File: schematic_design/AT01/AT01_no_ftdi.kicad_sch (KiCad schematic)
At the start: 66 parts, among them J1 JST Connector, J2 USB_C_Receptacle_USB2.0, J3 Conn_01x08, J4 Solenoid Valve Connector, J5 DC Pump Connector, Q1 DMG2301L, Q2 FDS6375, SW1 SW_Push, SW2 SW_Push, SW3 SW_Push, SW4 SW_Push, U1 MPRLS0025PA00001A, U2 LT1935ES5-TRPBF, U3 MCP73844T-840I/MS, U4 LM1117MP-3.3, U5 DRV8833PW, U6 ESP32-WROOM-32

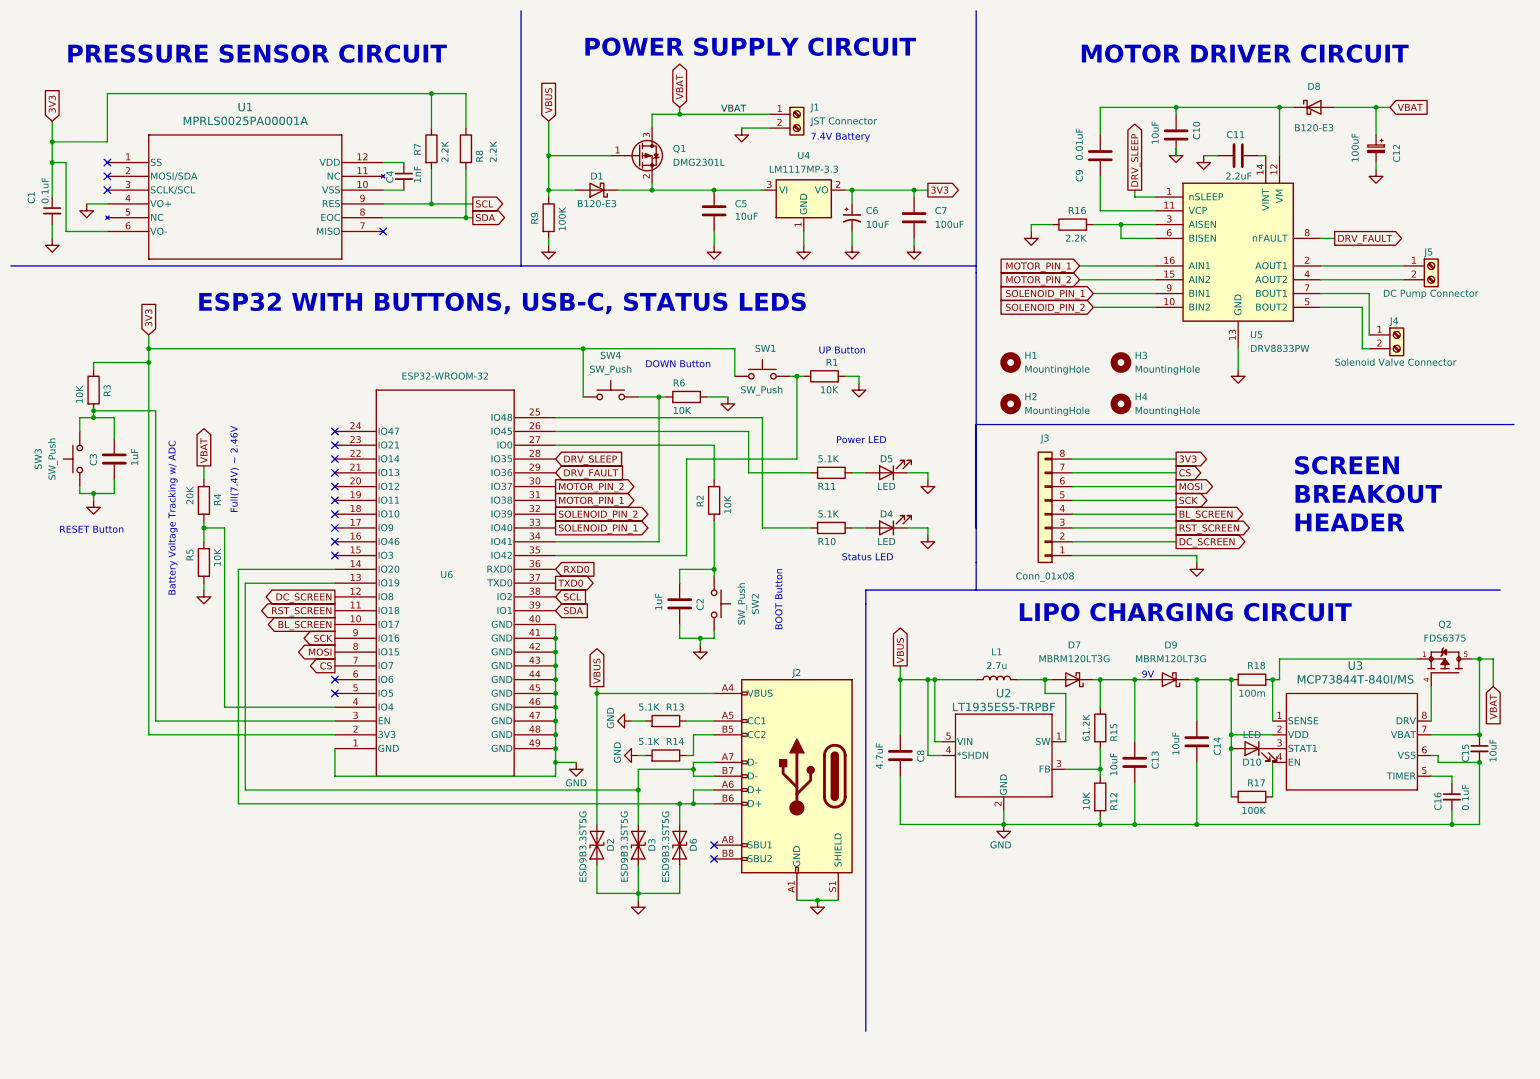
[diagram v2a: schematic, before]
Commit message: PCB redesign for new charging circuit with Espressif recommendations
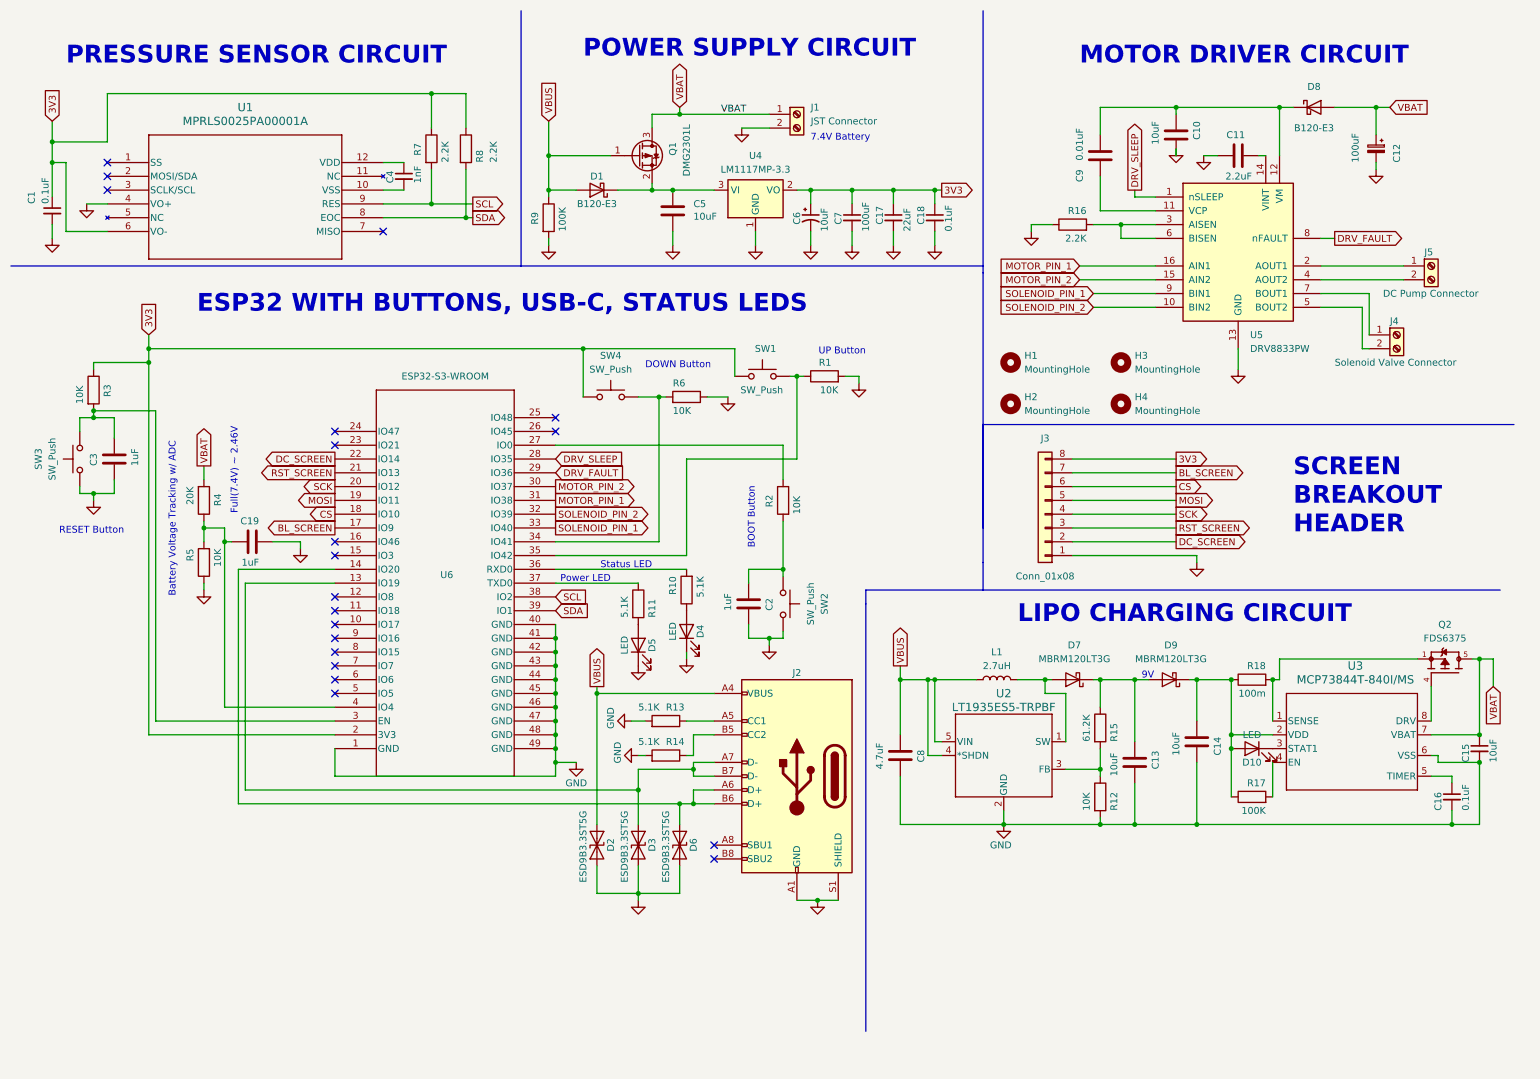
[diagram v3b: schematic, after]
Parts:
- removed C7: 100uF, Capacitor_SMD:C_0603_1608Metric_Pad1.08x0.95mm_HandSolder, symbol Device:C
- added C17: 22uF, Capacitor_SMD:C_0603_1608Metric_Pad1.08x0.95mm_HandSolder, symbol Device:C_Small
- added C18: 0.1uF, Capacitor_SMD:C_0603_1608Metric_Pad1.08x0.95mm_HandSolder, symbol Device:C_Small
- added C19: 1uF, Capacitor_SMD:C_0603_1608Metric_Pad1.08x0.95mm_HandSolder, symbol Device:C
- added C7: 100uF, Capacitor_SMD:C_0603_1608Metric_Pad1.08x0.95mm_HandSolder, symbol Device:C_Small
- J4, J5: footprint TerminalBlock:TerminalBlock_Altech_AK300-2_P5.00mm -> TerminalBlock_4Ucon:TerminalBlock_4Ucon_1x02_P3.50mm_Horizontal
- L1: value 2.7u -> 2.7uH; footprint (none) -> Library:IND_R2NC_SUM
- Q2: footprint FDS6375:SOIC127P600X175-8N -> Library:SOIC127P600X175-8N
- U6: value ESP32-WROOM-32 -> ESP32-S3-WROOM
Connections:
- net TXD0 is gone; now on an unnamed net: U6.37 (TXD0)
- net 3V3: now also C17.1, C18.1, C7.1
- net BL_SCREEN: now also J3.7 (Pin_7), U6.17 (IO9); no longer J3.4 (Pin_4), U6.10 (IO17)
- net CS: now also J3.6 (Pin_6), U6.18 (IO10); no longer J3.7 (Pin_7), U6.7 (IO7)
- net DC_SCREEN: now also U6.22 (IO14); no longer U6.12 (IO8)
- net GND: now also C17.2, C18.2, C19.2, C7.2
- net MOSI: now also J3.5 (Pin_5), U6.19 (IO11); no longer J3.6 (Pin_6), U6.8 (IO15)
- net RST_SCREEN: now also U6.21 (IO13); no longer U6.11 (IO18)
- net SCK: now also J3.4 (Pin_4), U6.20 (IO12); no longer J3.5 (Pin_5), U6.9 (IO16)
- net at U6.25 (IO48): no longer R10.2
- net at U6.26 (IO45): no longer R11.2
- net at R4.1, R5.2, U6.4 (IO4): now also C19.1
- net at R11.1: no longer D5.2 (A)
- net RXD0: no longer names the net of U6.36 (RXD0)
- net RXD0: now also R10.2
- new net: D5.2 (A), R11.2
- no-connect marks 18 -> 20
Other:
- moved on the sheet: C2, C5, C6, D4, R10, R2, SW2, U4

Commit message: adding design recommendations from call with Yi
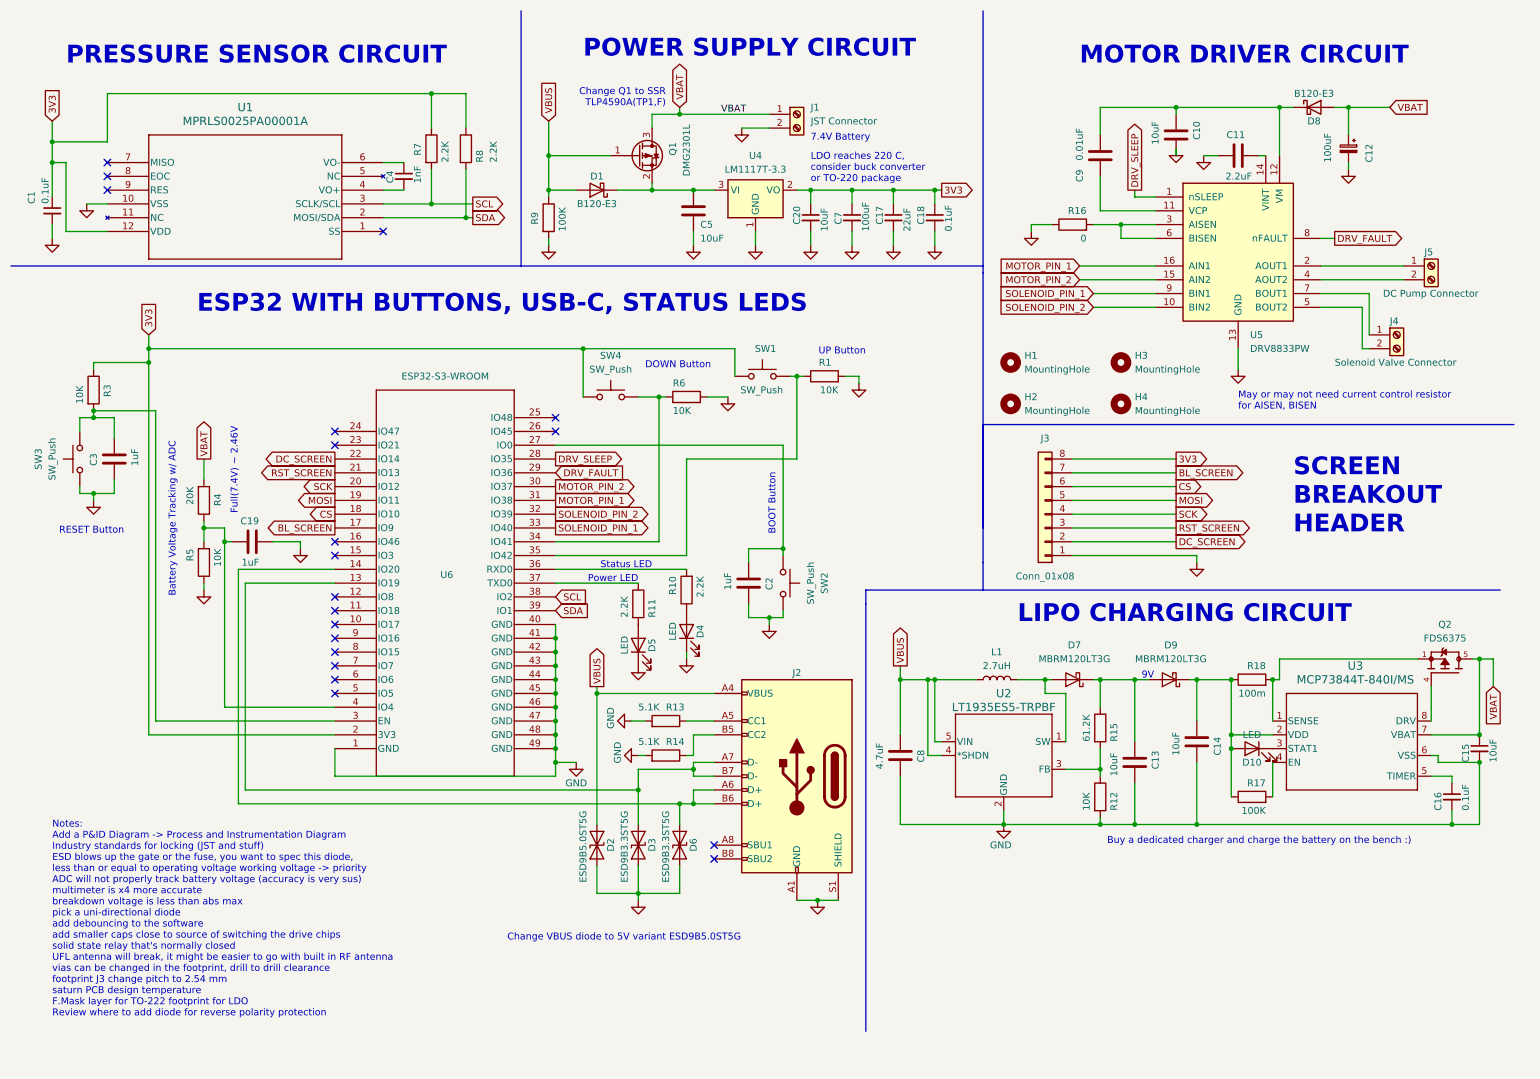
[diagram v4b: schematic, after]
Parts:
- removed C6: 10uF, Capacitor_SMD:C_1206_3216Metric_Pad1.33x1.80mm_HandSolder, symbol Device:C_Polarized_Small_US
- removed R2: 10K, Resistor_SMD:R_0603_1608Metric_Pad0.98x0.95mm_HandSolder, symbol Device:R
- added C20: 10uF, Capacitor_SMD:C_0603_1608Metric_Pad1.08x0.95mm_HandSolder, symbol Device:C_Small
- D2: value ESD9B3.3ST5G -> ESD9B5.0ST5G; symbol Diode:ESD9B3.3ST5G -> Diode:ESD9B5.0ST5G
- J3: footprint Connector_PinHeader_1.00mm:PinHeader_1x08_P1.00mm_Vertical -> Connector_PinHeader_2.54mm:PinHeader_1x08_P2.54mm_Vertical
- R10, R11: value 5.1K -> 2.2K
- R16: value 2.2K -> 0
- U4: value LM1117MP-3.3 -> LM1117T-3.3; footprint Package_TO_SOT_SMD:SOT-223-3_TabPin2 -> Package_TO_SOT_THT:TO-220-3_Horizontal_TabDown; symbol Regulator_Linear:LM1117MP-3.3 -> Regulator_Linear:LM1117T-3.3
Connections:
- net 3V3: now also U1.12 (VDD), C20.1; no longer U1.6 (VO-)
- net GND: now also U1.10 (VSS), C20.2; no longer U1.4 (VO+)
- net SCL: now also U1.3 (SCLK/SCL); no longer U1.9 (RES)
- net SDA: now also U1.2 (MOSI/SDA); no longer U1.8 (EOC)
- net at U6.27 (IO0): now also C2.1, SW2.1
- net at C4.2: now also U1.4 (VO+); no longer U1.10 (VSS)
- net at C4.1: now also U1.6 (VO-); no longer U1.12 (VDD)
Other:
- note added: "Buy a dedicated charger and charge the battery on the bench :)"
- note added: "Change Q1 to SSR TLP4590A(TP1,F)"
- note added: "Change VBUS diode to 5V variant ESD9B5.0ST5G"
- note added: "LDO reaches 220 C, consider buck converter or TO-220 package"
- note added: "May or may not need current control resistor for AISEN, BISEN"
- note added: "Notes: Add a P&ID Diagram -> Process and Instrumentation Diagram Industry standards for locking (JST and stuff) ESD blows up the gate or the fuse, you want to spec this diode, less than or equal to operating voltage working voltage -> priority ADC will not properly track battery voltage (accuracy is very sus) multimeter is x4 more accurate breakdown voltage is less than abs max pick a uni-directi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"
- moved on the sheet: C12, C2, C5, SW2, U1

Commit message: adding SSR and new ESD protection diodes according to design review
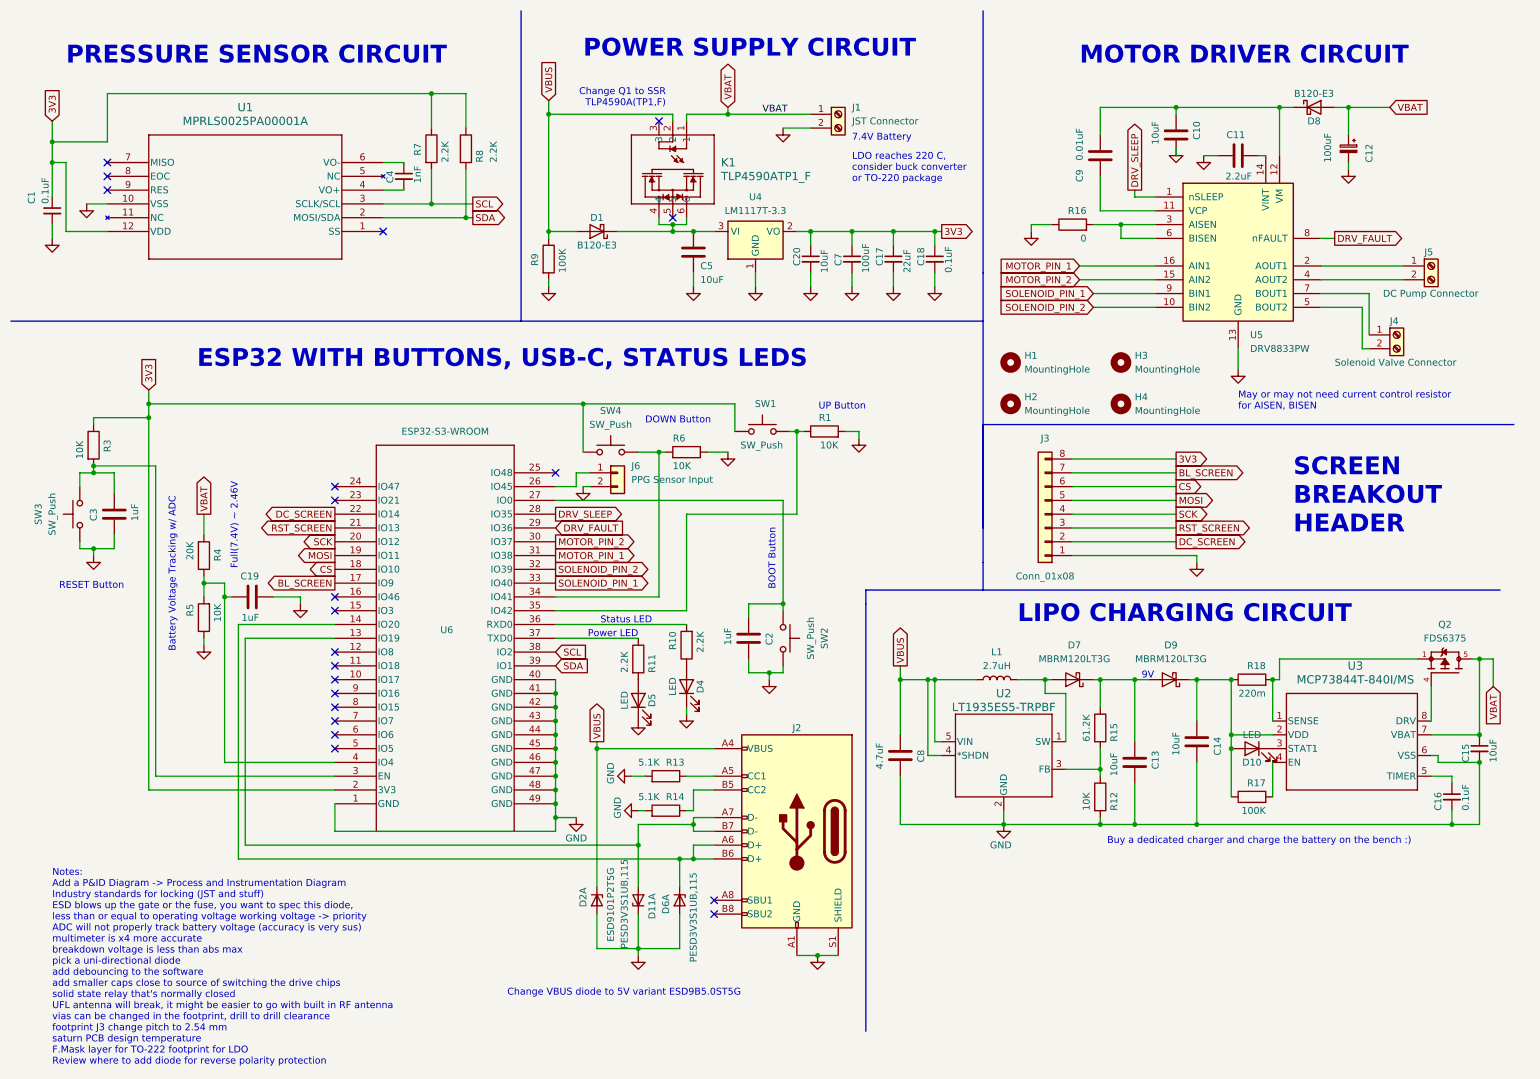
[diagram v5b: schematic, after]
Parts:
- removed D2: ESD9B5.0ST5G, Diode_SMD:D_SOD-923, symbol Diode:ESD9B5.0ST5G
- removed D3, D6: ESD9B3.3ST5G, Diode_SMD:D_SOD-923, symbol Diode:ESD9B3.3ST5G
- removed Q1: DMG2301L, Package_TO_SOT_SMD:SOT-23, symbol Transistor_FET:DMG2301L
- added D11, D6: PESD3V3S1UB,115, Diode_SMD:D_SOD-523, symbol Power_Protection:PESD3V3L4UF
- added D2: ESD9101P2T5G, Diode_SMD:D_SOD-923, symbol Power_Protection:PESD3V3L4UF
- added J6: PPG Sensor Input, Connector_PinSocket_2.54mm:PinSocket_1x02_P2.54mm_Vertical, symbol Connector_Generic:Conn_01x02
- added K1: TLP4590ATP1_F, Library:11-7A801S_TOS, symbol 2023-10-27_15-39-09:TLP4590ATP1_F
- R18: value 100m -> 220m
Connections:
- net GND: now also D11.1 (K1), D2.2 (A), D2.5 (A), D6.2 (A), D6.5 (A), J6.2 (Pin_2)
- net VBAT: now also K1.1
- net VBUS: now also D2.1 (K1), K1.2
- net at C5.1, D1.1 (K), U4.3 (VI): now also K1.4, K1.6
- net at J2.A6 (D+), J2.B6 (D+), U6.14 (IO20): now also D6.1 (K1)
- net at J2.A7 (D-), J2.B7 (D-), U6.13 (IO19): now also D11.2 (A), D11.5 (A)
- net at U6.26 (IO45): now also J6.1 (Pin_1)
- no-connect marks 20 -> 21
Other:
- moved on the sheet: C17, C18, C19, C2, C20, C3, C5, C7, D1, D4, D5, J1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

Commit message: final rev1.0 design
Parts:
- removed D11, D6: PESD3V3S1UB,115, Diode_SMD:D_SOD-523, symbol Power_Protection:PESD3V3L4UF
- removed D2: ESD9101P2T5G, Diode_SMD:D_SOD-923, symbol Power_Protection:PESD3V3L4UF
- removed H4: MountingHole, MountingHole:MountingHole_2.2mm_M2_ISO7380, symbol Mechanical:MountingHole
- added D12, D2: PESD3V3S1UB,115, Diode_SMD:D_SOD-523, symbol Device:D_Zener
- added D3: ESD9101P2T5G, Diode_SMD:D_SOD-923, symbol Device:D_Zener
- added R2: 0, Resistor_SMD:R_0603_1608Metric_Pad0.98x0.95mm_HandSolder, symbol Device:R
- C7: footprint Capacitor_SMD:C_0603_1608Metric_Pad1.08x0.95mm_HandSolder -> Capacitor_SMD:C_0805_2012Metric_Pad1.18x1.45mm_HandSolder
- J6: footprint Connector_PinSocket_2.54mm:PinSocket_1x02_P2.54mm_Vertical -> Connector_PinHeader_2.54mm:PinHeader_1x02_P2.54mm_Vertical
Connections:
- net GND: now also D12.1 (K), D2.2 (A), D3.2 (A)
- net VBUS: now also D3.1 (K), R2.1; no longer K1.2
- net at J2.A7 (D-), J2.B7 (D-), U6.13 (IO19): now also D12.2 (A)
- net at J2.A6 (D+), J2.B6 (D+), U6.14 (IO20): now also D2.1 (K)
- new net: K1.2, R2.2
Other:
- moved on the sheet: H1, H2, H3
